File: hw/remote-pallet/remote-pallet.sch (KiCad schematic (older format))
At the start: 4 parts

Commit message: really commiting changes to the schematic this time
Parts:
- added Q0: Q_NMOS_DGS, symbol Q_NMOS_DGS
- added Q1: Q_PMOS_DGS, symbol Q_PMOS_DGS
- added R0, R1, R5, R6, R7, R8, R9: R, symbol R
- added SW0: Arm Hardware, symbol SPST
- added U1: IOT-Photon-Headers, IOT-PHOTON-Headers, symbol IOT-Photon-Headers
- gave numbers to parts that had none: 4
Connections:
- net labels added: Armed, Fire0, Fire1, Fire2, Fire3, Fire4, Fire5, Fire6, Fire7, Sense0, Sense1, Sense2, Sense3, Sense4, Sense5, Sense6, Sense7, SenseSwitch, VCCsense
- wire segments 24 -> 123
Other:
- moved on the sheet: U0

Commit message: adding second switch
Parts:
- removed Q0: Q_NMOS_DGS, symbol Q_NMOS_DGS
- removed R0, R1: R, symbol R
- added SW?: Power, symbol SPST
- added U3: LM1084IS-3.3/NOPB, TO-263, symbol LM1084IS-3.3/NOPB
- renumbered R2 to R1, R3 to R2, R4 to R3, R5 to R4, R6 to R5, R7 to R6, R8 to R7, R9 to R8, SW0 to SW1, U0 to U1, U1 to U2
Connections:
- wire segments 123 -> 115
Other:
- moved on the sheet: Q1, U1

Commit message: updating schematic and starting board layout
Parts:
- removed R1, R2, R3, R4, R5, R6, R7, R8: R, symbol R
- removed U2: IOT-Photon-Headers, IOT-PHOTON-Headers, symbol IOT-Photon-Headers
- added C1, C2, C3, C4: 10uF, Capacitors_SMD:C_0805_HandSoldering, symbol CP1
- added M0, M1, M2, M3, M4, M5, M6, M7: E-MATCH, Terminal_Blocks:TerminalBlock_Pheonix_PT-3.5mm_2pol, symbol TEST
- added U2: PHOTON, particle-boards:PHOTON, symbol PHOTON
- Q1: footprint (none) -> TO_SOT_Packages_SMD:TO-252-2Lead
- SW1: renamed from SW?; footprint (none) -> M2011LL1W01-switch:M2011LL1W01
- SW2: renamed from SW1; footprint (none) -> M2011LL1W01-switch:M2011LL1W01
- U1, U3: footprint TO-263 -> TO_SOT_Packages_SMD:TO-263-3Lead
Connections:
- wire segments 115 -> 103
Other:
- moved on the sheet: SW1

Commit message: updating schematic and pcb
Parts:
- added J1: Power, symbol JACK_2P
- Q1: value Q_PMOS_DGS -> EMatch Test; footprint TO_SOT_Packages_SMD:TO-252-2Lead -> TO_SOT_Packages_SMD:SOT-23
- U1: value LM1084IS-3.3/NOPB -> Photon Power
- U3: value LM1084IS-3.3/NOPB -> Armed Sense
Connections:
- net 12V: now also J1.3
- net GND: now also J1.1, J1.2
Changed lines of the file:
@@
 LIBS:contrib
 LIBS:valves
-LIBS:iot_photon_headers
 LIBS:particle-boards
 LIBS:remote-pallet-cache
@@
 P 2350 1000
 F 0 "U1" H 2550 800 50  0000 C CNN
-F 1 "LM1084IS-3.3/NOPB" H 2050 1200 50  0000 L CNN
+F 1 "Photon Power" H 2050 1200 50  0000 L CNN
 F 2 "TO_SOT_Packages_SMD:TO-263-3Lead" H 2350 1100 50  0000 C CIN
 F 3 "" H 2350 1000 50  0000 C CNN
@@
 P 4350 1250
 F 0 "Q1" H 4650 1300 50  0000 R CNN
-F 1 "Q_PMOS_DGS" H 5000 1200 50  0000 R CNN
-F 2 "TO_SOT_Packages_SMD:TO-252-2Lead" H 4550 1350 50  0000 C CNN
+F 1 "EMatch Test" H 5000 1200 50  0000 R CNN
+F 2 "TO_SOT_Packages_SMD:SOT-23" H 4550 1350 50  0000 C CNN
 F 3 "" H 4350 1250 50  0000 C CNN
 	1    4350 1250
@@
 P 6300 850
 F 0 "U3" H 6500 650 50  0000 C CNN
-F 1 "LM1084IS-3.3/NOPB" H 6000 1050 50  0000 L CNN
+F 1 "Armed Sense" H 6000 1050 50  0000 L CNN
 F 2 "TO_SOT_Packages_SMD:TO-263-3Lead" H 6300 950 50  0000 C CIN
 F 3 "" H 6300 850 50  0000 C CNN
@@
 Wire Wire Line
 	5050 4700 5200 4700
+Text GLabel 2600 5050 2    60   Input ~ 0
+12V
+$Comp
+L GND #PWR020
+U 1 1 56EC8173
+P 2700 5450
+F 0 "#PWR020" H 2700 5200 50  0001 C CNN
+F 1 "GND" H 2700 5300 50  0000 C CNN
+F 2 "" H 2700 5450 50  0000 C CNN
+F 3 "" H 2700 5450 50  0000 C CNN
+	1    2700 5450
+	1    0    0    -1
+$EndComp
+Wire Wire Line
+	2600 5200 2700 5200
+Wire Wire Line
+	2700 5200 2700 5450
+Wire Wire Line
+	2600 5300 2700 5300
+Connection ~ 2700 5300
+$Comp
+L JACK_2P J1
+U 1 1 56EC9DB9
+P 2150 5200
+F 0 "J1" H 1800 5000 50  0000 C CNN
+F 1 "Power" H 2000 5450 50  0000 C CNN
+F 2 "" H 2150 5200 50  0000 C CNN
+F 3 "" H 2150 5200 50  0000 C CNN
+	1    2150 5200
+	1    0    0    -1
+$EndComp
 $EndSCHEMATC

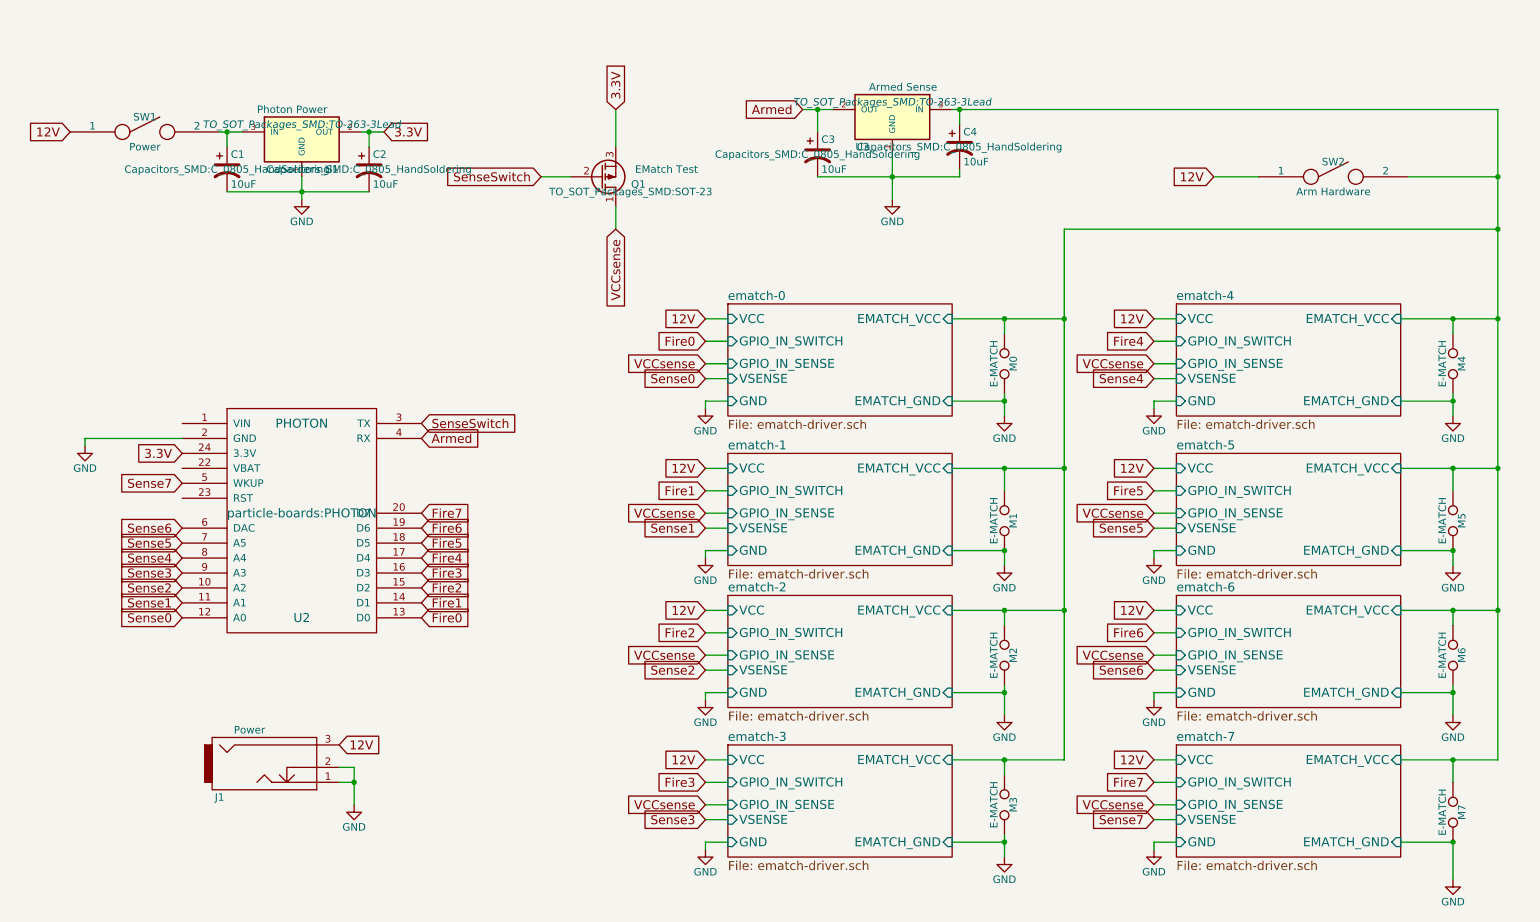
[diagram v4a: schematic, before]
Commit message: adding some new footprints, laying out board
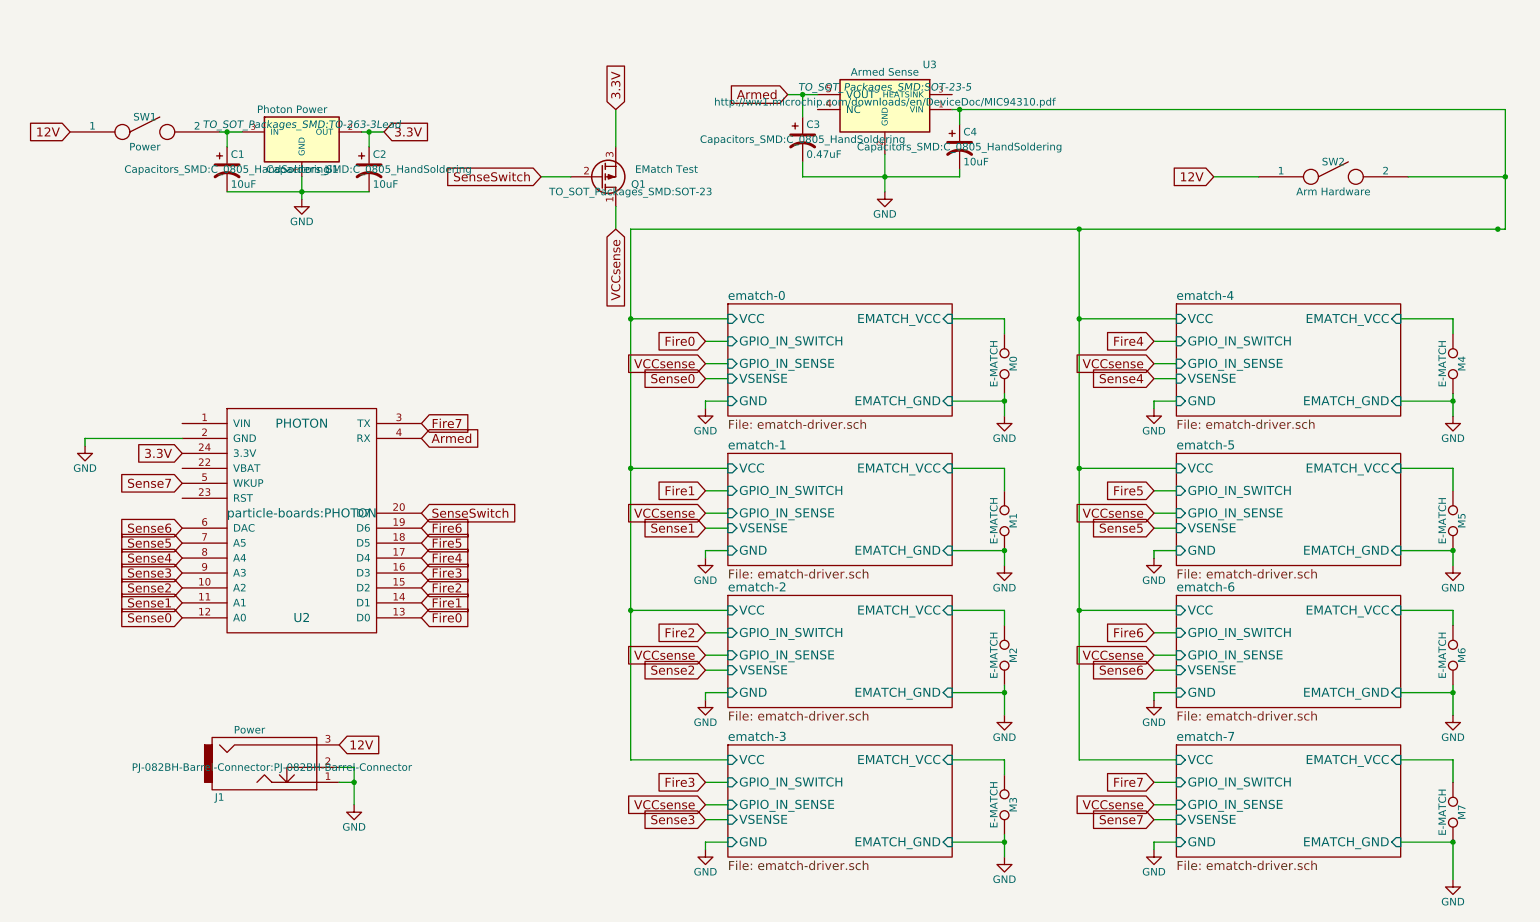
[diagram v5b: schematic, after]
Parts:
- removed U3: Armed Sense, TO_SOT_Packages_SMD:TO-263-3Lead, symbol LM1084IS-3.3/NOPB
- added U3: Armed Sense, TO_SOT_Packages_SMD:SOT-23-5, symbol MIC94310-SYM5-TR
- C3: value 10uF -> 0.47uF; type tantalum -> low-esr ceramic
- C4: type tantalum -> low-esr ceramic
- J1: footprint (none) -> PJ-082BH-Barrel-Connector:PJ-082BH-Barrel-Connector
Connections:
- net Armed: now also U3.5 (VOUT)
- net Fire7: now also U2.3 (TX); no longer U2.20 (D7)
- net GND: now also U3.2 (GND)
- net SenseSwitch: now also U2.20 (D7); no longer U2.3 (TX)
- net ematch-0/EMATCH_VCC: no longer C4.1, M1.1, M2.1, M3.1, M4.1, M5.1, M6.1, M7.1, SW2.2
- new net ematch-0/VCC: C4.1, SW2.2, U3.1 (VIN)
- new net ematch-1/EMATCH_VCC: M1.1
- new net ematch-2/EMATCH_VCC: M2.1
- new net ematch-3/EMATCH_VCC: M3.1
- new net ematch-4/EMATCH_VCC: M4.1
- new net ematch-5/EMATCH_VCC: M5.1
- new net ematch-6/EMATCH_VCC: M6.1
- new net ematch-7/EMATCH_VCC: M7.1
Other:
- moved on the sheet: C3
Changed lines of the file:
@@
 LIBS:valves
 LIBS:particle-boards
+LIBS:IC REG LDO 3.3V 0.2A SOT23-5
 LIBS:remote-pallet-cache
 EELAYER 25 0
@@
 F8 "GND" I L 5200 4700 60
 $EndSheet
-Text GLabel 5050 2200 0    60   Input ~ 0
-12V
-Text GLabel 5050 3200 0    60   Input ~ 0
-12V
 $Comp
 L GND #PWR02
@@
 	1    0    0    -1
 $EndComp
-Text GLabel 5050 4150 0    60   Input ~ 0
-12V
 Text GLabel 800  950  0    60   Input ~ 0
 12V
@@
 	1    0    0    -1
 $EndComp
-Text GLabel 5050 5150 0    60   Input ~ 0
-12V
 $Sheet
 S 8200 2100 1500 750
@@
 F8 "GND" I L 8200 4700 60
 $EndSheet
-Text GLabel 8050 2200 0    60   Input ~ 0
-12V
-Text GLabel 8050 3200 0    60   Input ~ 0
-12V
 $Comp
 L GND #PWR06
@@
 	1    0    0    -1
 $EndComp
-Text GLabel 8050 4150 0    60   Input ~ 0
-12V
 $Sheet
 S 8200 5050 1500 750
@@
 	1    0    0    -1
 $EndComp
-Text GLabel 8050 5150 0    60   Input ~ 0
-12V
 $Comp
 L SPST SW2
@@
 Text GLabel 4450 1600 3    60   Input ~ 0
 VCCsense
-Text GLabel 5700 800  0    60   Input ~ 0
+Text GLabel 5600 700  0    60   Input ~ 0
 Armed
 Text GLabel 3950 1250 0    60   Input ~ 0
@@
 Text GLabel 3150 3600 2    60   Input ~ 0
 Fire6
-Text GLabel 3150 3500 2    60   Input ~ 0
+Text GLabel 3150 2900 2    60   Input ~ 0
 Fire7
 Text GLabel 1550 4200 0    60   Input ~ 0
@@
 Text GLabel 1550 3300 0    60   Input ~ 0
 Sense7
-Text GLabel 3150 2900 2    60   Input ~ 0
+Text GLabel 3150 3500 2    60   Input ~ 0
 SenseSwitch
 Text GLabel 3150 3000 2    60   Input ~ 0
@@
 3.3V
 $Comp
-L LM1084IS-3.3/NOPB U3
-U 1 1 56EB16BF
-P 6300 850
-F 0 "U3" H 6500 650 50  0000 C CNN
-F 1 "Armed Sense" H 6000 1050 50  0000 L CNN
-F 2 "TO_SOT_Packages_SMD:TO-263-3Lead" H 6300 950 50  0000 C CIN
-F 3 "" H 6300 850 50  0000 C CNN
-	1    6300 850
-	-1   0    0    -1
-$EndComp
-$Comp
 L GND #PWR019
 U 1 1 56EB2D78
-P 6300 1400
-F 0 "#PWR019" H 6300 1150 50  0001 C CNN
-F 1 "GND" H 6300 1250 50  0000 C CNN
-F 2 "" H 6300 1400 50  0000 C CNN
-F 3 "" H 6300 1400 50  0000 C CNN
-	1    6300 1400
+P 6250 1350
+F 0 "#PWR019" H 6250 1100 50  0001 C CNN
+F 1 "GND" H 6250 1200 50  0000 C CNN
+F 2 "" H 6250 1350 50  0000 C CNN
+F 3 "" H 6250 1350 50  0000 C CNN
+	1    6250 1350
 	1    0    0    -1
 $EndComp
@@
 L CP1 C3
 U 1 1 56EDA658
-P 5800 1100
-F 0 "C3" H 5825 1200 50  0000 L CNN
-F 1 "10uF" H 5825 1000 50  0000 L CNN
-F 2 "Capacitors_SMD:C_0805_HandSoldering" H 5800 1100 50  0000 C CNN
-F 3 "" H 5800 1100 50  0000 C CNN
-F 4 "tantalum" H 5800 1100 60  0001 C CNN "type"
-	1    5800 1100
+P 5700 1000
+F 0 "C3" H 5725 1100 50  0000 L CNN
+F 1 "0.47uF" H 5725 900 50  0000 L CNN
+F 2 "Capacitors_SMD:C_0805_HandSoldering" H 5700 1000 50  0000 C CNN
+F 3 "" H 5700 1000 50  0000 C CNN
+F 4 "low-esr ceramic" H 5700 1000 60  0001 C CNN "type"
+	1    5700 1000
 	1    0    0    -1
 $EndComp
@@
 F 2 "Capacitors_SMD:C_0805_HandSoldering" H 6750 1050 50  0000 C CNN
 F 3 "" H 6750 1050 50  0000 C CNN
-F 4 "tantalum" H 6750 1050 60  0001 C CNN "type"
+F 4 "low-esr ceramic" H 6750 1050 60  0001 C CNN "type"
 	1    6750 1050
 	1    0    0    -1
@@
 	2350 1400 2350 1250
 Wire Wire Line
-	6700 2200 7450 2200
-Wire Wire Line
 	7050 2200 7050 2300
 Wire Wire Line
-	7450 3200 6700 3200
-Wire Wire Line
 	7050 3200 7050 3350
 Wire Wire Line
 	7050 3750 6700 3750
 Wire Wire Line
-	7450 4150 6700 4150
-Wire Wire Line
 	7050 4150 7050 4250
 Wire Wire Line
 	7050 4700 6700 4700
 Wire Wire Line
-	5050 2200 5200 2200
-Wire Wire Line
-	5050 3200 5200 3200
+	4550 2200 5200 2200
+Wire Wire Line
+	4550 3200 5200 3200
 Wire Wire Line
 	5050 2800 5050 2750
@@
 	5050 3750 5200 3750
 Wire Wire Line
-	5050 4150 5200 4150
-Wire Wire Line
-	7450 5150 6700 5150
+	4550 4150 5200 4150
 Wire Wire Line
 	7050 5150 7050 5250
@@
 	5050 5700 5200 5700
 Wire Wire Line
-	5050 5150 5200 5150
-Wire Wire Line
-	9700 2200 10350 2200
+	4550 5150 5200 5150
 Wire Wire Line
 	10050 2200 10050 2300
@@
 	10050 2750 9700 2750
 Wire Wire Line
-	10350 3200 9700 3200
-Wire Wire Line
 	10050 3200 10050 3350
 Wire Wire Line
 	10050 3750 9700 3750
 Wire Wire Line
-	10350 4150 9700 4150
-Wire Wire Line
 	10050 4150 10050 4250
 Wire Wire Line
 	10050 4700 9700 4700
 Wire Wire Line
-	8050 2200 8200 2200
-Wire Wire Line
-	8050 3200 8200 3200
+	7550 2200 8200 2200
+Wire Wire Line
+	7550 3200 8200 3200
 Wire Wire Line
 	8050 3800 8050 3750
@@
 	8050 3750 8200 3750
 Wire Wire Line
-	8050 4150 8200 4150
-Wire Wire Line
-	10350 5150 9700 5150
+	7550 4150 8200 4150
 Wire Wire Line
 	10050 5150 10050 5300
@@
 	8050 5700 8200 5700
 Wire Wire Line
-	8050 5150 8200 5150
-Wire Wire Line
-	9750 1250 10350 1250
-Wire Wire Line
-	10350 800  10350 5150
-Connection ~ 10050 2200
-Connection ~ 10050 3200
-Connection ~ 10350 2200
-Connection ~ 10050 4150
-Connection ~ 10350 3200
-Connection ~ 10050 5150
-Connection ~ 10350 4150
-Wire Wire Line
-	10350 1600 7450 1600
-Wire Wire Line
-	7450 1600 7450 5150
-Connection ~ 7050 2200
+	7550 5150 8200 5150
+Wire Wire Line
+	9750 1250 10400 1250
+Wire Wire Line
+	4550 1600 10400 1600
 Connection ~ 10350 1600
-Connection ~ 7050 3200
-Connection ~ 7450 2200
-Connection ~ 7050 4150
-Connection ~ 7450 3200
-Connection ~ 7050 5150
-Connection ~ 7450 4150
 Connection ~ 10050 2750
 Connection ~ 10050 3750
@@
 Connection ~ 7050 3750
 Wire Wire Line
-	6700 800  10350 800
-Connection ~ 10350 1250
+	6700 800  10400 800
 Wire Wire Line
 	8450 1250 8750 1250
@@
 	8050 4700 8200 4700
 Wire Wire Line
-	6300 1100 6300 1400
-Wire Wire Line
-	5900 800  5700 800
-Wire Wire Line
-	5800 800  5800 950
-Connection ~ 5800 800
-Wire Wire Line
-	5800 1250 6750 1250
-Connection ~ 6300 1250
+	5800 700  5600 700
+Wire Wire Line
+	5700 700  5700 850
+Connection ~ 5700 700
+Wire Wire Line
+	5700 1250 6750 1250
 Wire Wire Line
 	6750 1250 6750 1200
@@
 F 0 "J1" H 1800 5000 50  0000 C CNN
 F 1 "Power" H 2000 5450 50  0000 C CNN
-F 2 "" H 2150 5200 50  0000 C CNN
+F 2 "PJ-082BH-Barrel-Connector:PJ-082BH-Barrel-Connector" H 2150 5200 50  0000 C CNN
 F 3 "" H 2150 5200 50  0000 C CNN
 	1    2150 5200
 	1    0    0    -1
 $EndComp
+$Comp
+L MIC94310-SYM5-TR U3
+U 1 1 56ECD499
+P 6250 750
+F 0 "U3" H 5950 1000 50  0000 C CNN
+F 1 "Armed Sense" H 6250 950 50  0000 C CNN
+F 2 "TO_SOT_Packages_SMD:SOT-23-5" H 6250 850 50  0000 C CIN
+F 3 "http://ww1.microchip.com/downloads/en/DeviceDoc/MIC94310.pdf" H 6250 750 50  0000 C CNN
+	1    6250 750
+	-1   0    0    -1
+$EndComp
+Wire Wire Line
+	5700 1150 5700 1250
+Wire Wire Line
+	6250 1100 6250 1350
+Connection ~ 6250 1250
+Wire Wire Line
+	10400 800  10400 1600
+Connection ~ 10400 1250
+Wire Wire Line
+	4550 1600 4550 5150
+Connection ~ 4550 2200
+Connection ~ 4550 3200
+Connection ~ 4550 4150
+Wire Wire Line
+	7550 1600 7550 5150
+Connection ~ 7550 1600
+Connection ~ 7550 2200
+Connection ~ 7550 3200
+Connection ~ 7550 4150
+Wire Wire Line
+	6700 2200 7050 2200
+Wire Wire Line
+	6700 3200 7050 3200
+Wire Wire Line
+	6700 4150 7050 4150
+Wire Wire Line
+	6700 5150 7050 5150
+Wire Wire Line
+	9700 5150 10050 5150
+Wire Wire Line
+	9700 4150 10050 4150
+Wire Wire Line
+	9700 3200 10050 3200
+Wire Wire Line
+	9700 2200 10050 2200
 $EndSCHEMATC

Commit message: changes to layout adding debug LEDs
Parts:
- added LED1: Battery, LEDs:LED_0603, symbol LED
- added LED2: 3.3, LEDs:LED_0603, symbol LED
- added LED3: Armed, LEDs:LED_0603, symbol LED
- added R1, R3: 600, Resistors_SMD:R_0603_HandSoldering, symbol R
- added R2: 165, Resistors_SMD:R_0603_HandSoldering, symbol R
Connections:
- net 12V: now also LED1.2 (A); no longer SW2.1
- net 3.3V: now also LED2.2 (A)
- net GND: now also R1.2, R2.2, R3.2
- net ematch-0/VCC: now also LED3.2 (A)
- net 12VSwitched: now reaches C1.1, SW1.2, U1.3 (IN)
- net 12VSwitched: now also SW2.1
- new net: LED1.1 (K), R1.1
- new net: LED2.1 (K), R2.1
- new net: LED3.1 (K), R3.1
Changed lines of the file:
@@
 	1    0    0    -1
 $EndComp
-Text GLabel 800  950  0    60   Input ~ 0
+Text GLabel 750  950  0    60   Input ~ 0
 12V
 Text GLabel 2900 950  2    60   Input ~ 0
@@
 	1    0    0    -1
 $EndComp
-Text GLabel 8450 1250 0    60   Input ~ 0
-12V
 $Comp
 L GND #PWR010
@@
 Wire Wire Line
 	4550 1600 10400 1600
-Connection ~ 10350 1600
 Connection ~ 10050 2750
 Connection ~ 10050 3750
@@
 Connection ~ 6250 1250
 Wire Wire Line
-	10400 800  10400 1600
+	10400 800  10400 1650
 Connection ~ 10400 1250
 Wire Wire Line
@@
 Wire Wire Line
 	9700 2200 10050 2200
+Text GLabel 1850 950  1    60   Input ~ 0
+12VSwitched
+Text GLabel 8450 1250 0    60   Input ~ 0
+12VSwitched
+$Comp
+L LED LED1
+U 1 1 56EF3A6F
+P 800 1300
+F 0 "LED1" H 800 1400 50  0000 C CNN
+F 1 "Battery" H 800 1200 50  0000 C CNN
+F 2 "LEDs:LED_0603" H 800 1300 50  0000 C CNN
+F 3 "" H 800 1300 50  0000 C CNN
+	1    800  1300
+	0    -1   -1   0
+$EndComp
+$Comp
+L LED LED2
+U 1 1 56EF3C14
+P 1300 1750
+F 0 "LED2" H 1300 1850 50  0000 C CNN
+F 1 "3.3" H 1300 1650 50  0000 C CNN
+F 2 "LEDs:LED_0603" H 1300 1750 50  0000 C CNN
+F 3 "" H 1300 1750 50  0000 C CNN
+	1    1300 1750
+	0    -1   -1   0
+$EndComp
+$Comp
+L LED LED3
+U 1 1 56EF3DBF
+P 10400 1850
+F 0 "LED3" H 10400 1950 50  0000 C CNN
+F 1 "Armed" H 10400 1750 50  0000 C CNN
+F 2 "LEDs:LED_0603" H 10400 1850 50  0000 C CNN
+F 3 "" H 10400 1850 50  0000 C CNN
+	1    10400 1850
+	0    -1   -1   0
+$EndComp
+Wire Wire Line
+	750  950  800  950
+Wire Wire Line
+	800  950  800  1100
+$Comp
+L R R1
+U 1 1 56EF6CD9
+P 800 1650
+F 0 "R1" V 880 1650 50  0000 C CNN
+F 1 "600" V 800 1650 50  0000 C CNN
+F 2 "Resistors_SMD:R_0603_HandSoldering" V 730 1650 50  0000 C CNN
+F 3 "" H 800 1650 50  0000 C CNN
+	1    800  1650
+	1    0    0    -1
+$EndComp
+$Comp
+L R R3
+U 1 1 56EF6E8C
+P 10400 2200
+F 0 "R3" V 10480 2200 50  0000 C CNN
+F 1 "600" V 10400 2200 50  0000 C CNN
+F 2 "Resistors_SMD:R_0603_HandSoldering" V 10330 2200 50  0000 C CNN
+F 3 "" H 10400 2200 50  0000 C CNN
+	1    10400 2200
+	1    0    0    -1
+$EndComp
+$Comp
+L R R2
+U 1 1 56EF7031
+P 1300 2100
+F 0 "R2" V 1380 2100 50  0000 C CNN
+F 1 "165" V 1300 2100 50  0000 C CNN
+F 2 "Resistors_SMD:R_0603_HandSoldering" V 1230 2100 50  0000 C CNN
+F 3 "" H 1300 2100 50  0000 C CNN
+	1    1300 2100
+	1    0    0    -1
+$EndComp
+$Comp
+L GND #PWR021
+U 1 1 56EFCFF7
+P 800 1800
+F 0 "#PWR021" H 800 1550 50  0001 C CNN
+F 1 "GND" H 800 1650 50  0000 C CNN
+F 2 "" H 800 1800 50  0000 C CNN
+F 3 "" H 800 1800 50  0000 C CNN
+	1    800  1800
+	1    0    0    -1
+$EndComp
+$Comp
+L GND #PWR022
+U 1 1 56EFD24E
+P 1300 2250
+F 0 "#PWR022" H 1300 2000 50  0001 C CNN
+F 1 "GND" H 1300 2100 50  0000 C CNN
+F 2 "" H 1300 2250 50  0000 C CNN
+F 3 "" H 1300 2250 50  0000 C CNN
+	1    1300 2250
+	1    0    0    -1
+$EndComp
+$Comp
+L GND #PWR023
+U 1 1 56EFD3E4
+P 10400 2350
+F 0 "#PWR023" H 10400 2100 50  0001 C CNN
+F 1 "GND" H 10400 2200 50  0000 C CNN
+F 2 "" H 10400 2350 50  0000 C CNN
+F 3 "" H 10400 2350 50  0000 C CNN
+	1    10400 2350
+	1    0    0    -1
+$EndComp
+Text GLabel 1300 1550 1    60   Input ~ 0
+3.3V
+Connection ~ 10400 1600
 $EndSCHEMATC
